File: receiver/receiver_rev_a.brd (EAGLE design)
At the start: 100 x 80 mm, 1 part

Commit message: Mostly done with the receiver
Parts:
- added C1, C2, C3: 100uF, microbuilder:1206
- added C4: 0.1uF, microbuilder:0603-MINI
- added CN1: (no value), microbuilder:DCJACK_2MM_PTH
- added FID1, FID2, FID3, FID4, FID5, FID6: FIDUCIAL, adafruit:FIDUCIAL_1MM
- added FUSE: (no value), Custom:FUSE-HOLDER-3557
- added J1: POWERPOLE_POWER45A_HORIZONTAL_DRILL, powerpoles:POWERPOLE_PAIR_45A_HORIZ_HOLE
- added JP1: (no value), SparkFun-Connectors:1X04
- added JP2: (no value), SparkFun-Connectors:1X02_XTRA_BIG
- added OUT1, OUT2, OUT3: MC4, con-phoenix-381_l:MC4
- added Q1, Q2, Q3: (no value), Custom:SC59
- added R1, R10, R2, R3, R4, R5, R6, R7, R8, R9: 120, microbuilder:0603-MINI
- added R11, R12: 220, microbuilder:0603-MINI
- added R13, R14, R15: 10k, microbuilder:0603-MINI
- added SWITCH: (no value), Custom:194-DIP-SWITCH
- added U$2: (no value), Custom:AK-B-FT21
- added U$3, U$4, U$5, U$6: MOUNTINGHOLE2.5, microbuilder:MOUNTINGHOLE_2.5_PLATED
- added U$7: (no value), Custom:RJHSE-538X
- added U1: (no value), maxim:TSSOP16
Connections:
- new net A+: R1.2, U$7.1, U1.2
- new net A-: R1.1, U$7.2, U1.1
- new net B+: R2.2, U$7.3, U1.14
- new net B-: R2.1, U$7.6, U1.15
- new net C+: R3.2, U$7.4, U1.6
- new net C-: R3.1, U$7.5, U1.7
- new net CLOCK: JP1.1, R6.2, R7.2, R9.2, U1.11
- new net D+: R4.2, U$7.7, U1.10
- new net D-: R4.1, U$7.8, U1.9
- new net DATA1: JP1.4, R5.2, U1.3
- new net DATA2: JP1.3, R8.2, U1.13
- new net DATA3: JP1.2, R10.2, U1.5
- new net GATE1: Q1.G, R13.1, SWITCH.1B
- new net GATE2: Q2.G, R14.1, SWITCH.2B
- new net GATE3: Q3.G, R15.1, SWITCH.3B
- new net GND: C4.2, CN1.GND, J1.BLACK, JP2.2, Q1.S, Q2.S, Q3.S, R11.1, R12.1, R13.2, R14.2, R15.2, U$7.P$1, U$7.P$2, U1.8
- new net GNDBREAK: CN1.GNDBREAK
- new net N$1: OUT1.2, R5.1
- new net N$10: R11.2, U$7.9
- new net N$11: R12.2, U$7.11
- new net N$2: OUT1.3, R6.1
- new net N$3: C1.2, OUT1.4, Q1.D
- new net N$4: OUT2.2, R8.1
- new net N$5: OUT2.3, R7.1
- new net N$6: C2.2, OUT2.4, Q2.D
- new net N$7: OUT3.2, R10.1
- new net N$8: OUT3.3, R9.1
- new net N$9: C3.2, OUT3.4, Q3.D
- new net PREFUSE_VCC: CN1.PWR, FUSE.A1, FUSE.A2, J1.RED, JP2.1, U$7.12
- new net VCC: C1.1, C2.1, C3.1, C4.1, FUSE.B1, FUSE.B2, OUT1.1, OUT2.1, OUT3.1, SWITCH.1A, SWITCH.2A, SWITCH.3A, U$7.10, U1.12, U1.16, U1.4
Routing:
- net PREFUSE_VCC: track 0.00 -> 88.8 mm
- net CLOCK: track 0.00 -> 88.0 mm
- net DATA3: track 0.00 -> 64.9 mm, vias 0 -> 2
- net DATA2: track 0.00 -> 48.0 mm, vias 0 -> 2
- net VCC: track 0.00 -> 44.9 mm, vias 0 -> 2
- net GATE1: track 0.00 -> 44.3 mm
- net B+: track 0.00 -> 37.0 mm, vias 0 -> 2
- net GATE3: track 0.00 -> 36.2 mm
- net B-: track 0.00 -> 35.8 mm, vias 0 -> 2
- net GATE2: track 0.00 -> 29.9 mm
- net DATA1: track 0.00 -> 28.6 mm
- net A+: track 0.00 -> 23.7 mm
- net A-: track 0.00 -> 22.2 mm
- net D+: track 0.00 -> 19.4 mm
- net C-: track 0.00 -> 19.1 mm
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- added copper zone on layer 1, net GND
- added copper zone on layer 16, net VCC
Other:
- board size 100 x 80 mm -> 74 x 50.3 mm
- board text added: "5V"
- board text added: "CLCK"
- board text added: "DI1"
- board text added: "DI2"
- board text added: "DI3"
- board text added: "GND"

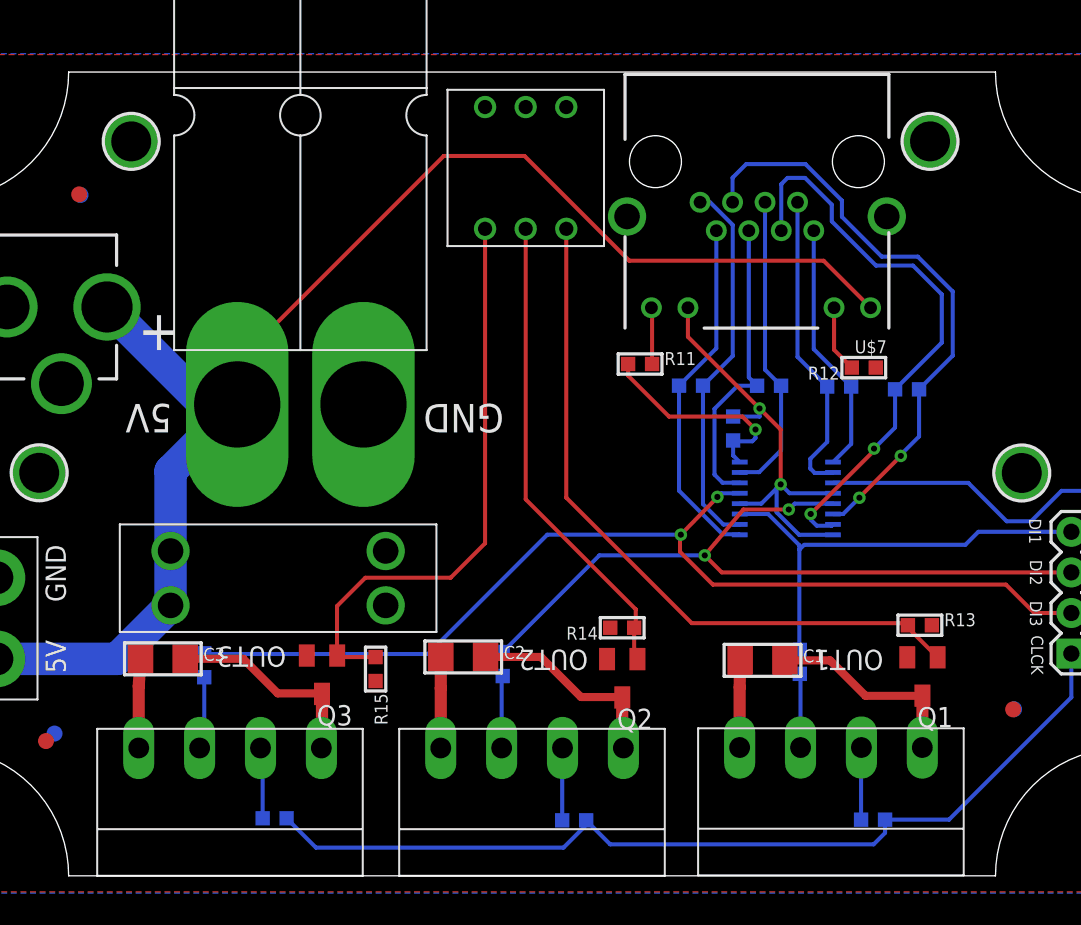
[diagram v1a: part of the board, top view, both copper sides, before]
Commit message: Almost done with cape routing
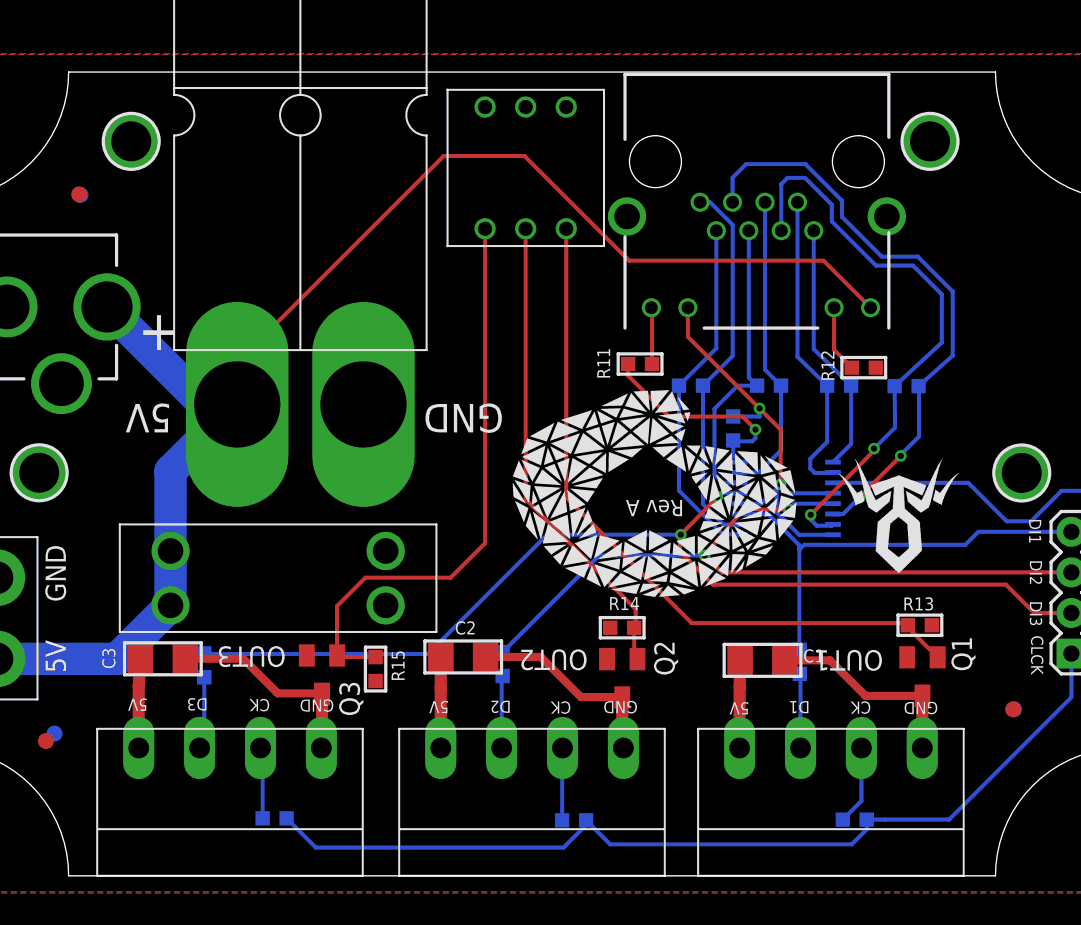
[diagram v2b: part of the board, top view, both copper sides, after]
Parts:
- moved R6 1.14 mm to (62.2, 7.52)
- moved R2 0.20 mm to (65.4, 34.6)
- moved R4 0.05 mm to (61.2, 34.7)
- renumbered U$7 to J2
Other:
- board text added: "2016"
- board text added: "CK"
- board text added: "D1"
- board text added: "D2"
- board text added: "D3"
- board text added: "Rev A"
- board text added: "Shlomo Zippel"
